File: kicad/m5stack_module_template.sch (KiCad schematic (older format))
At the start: 1 part

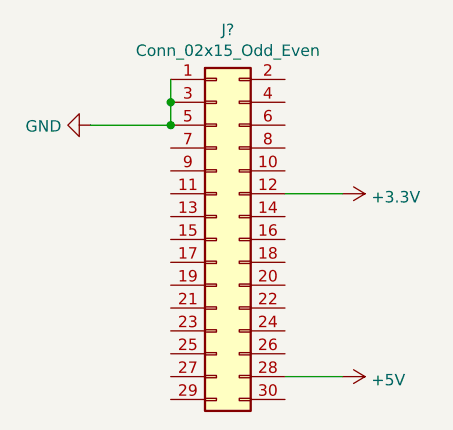
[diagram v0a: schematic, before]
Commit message: Create header footprint
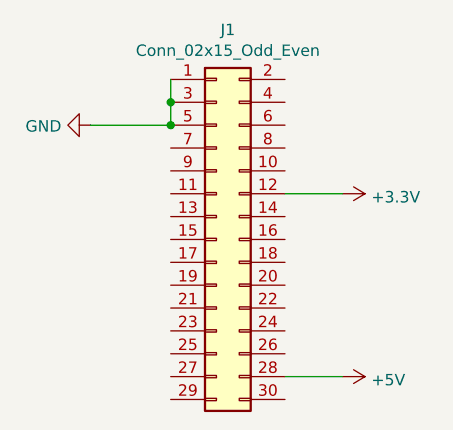
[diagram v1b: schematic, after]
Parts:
- J1: renamed from J?; footprint (none) -> M5Stack-Module-Template:M5Stack_PinHeader_2x15_P2.54mm
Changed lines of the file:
@@
 $EndDescr
 $Comp
-L Connector_Generic:Conn_02x15_Odd_Even J?
+L Connector_Generic:Conn_02x15_Odd_Even J1
 U 1 1 60196CD0
 P 1700 3000
-F 0 "J?" H 1750 3917 50  0000 C CNN
+F 0 "J1" H 1750 3917 50  0000 C CNN
 F 1 "Conn_02x15_Odd_Even" H 1750 3826 50  0000 C CNN
-F 2 "" H 1700 3000 50  0001 C CNN
+F 2 "M5Stack-Module-Template:M5Stack_PinHeader_2x15_P2.54mm" H 1700 3000 50  0001 C CNN
 F 3 "~" H 1700 3000 50  0001 C CNN
 	1    1700 3000

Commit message: Reorganize footprint library
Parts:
- J1: footprint M5Stack-Module-Template:M5Stack_PinHeader_2x15_P2.54mm -> lib:M5Stack_PinHeader_2x15_P2.54mm
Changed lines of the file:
@@
 F 0 "J1" H 1750 3917 50  0000 C CNN
 F 1 "Conn_02x15_Odd_Even" H 1750 3826 50  0000 C CNN
-F 2 "M5Stack-Module-Template:M5Stack_PinHeader_2x15_P2.54mm" H 1700 3000 50  0001 C CNN
+F 2 "lib:M5Stack_PinHeader_2x15_P2.54mm" H 1700 3000 50  0001 C CNN
 F 3 "~" H 1700 3000 50  0001 C CNN
 	1    1700 3000
